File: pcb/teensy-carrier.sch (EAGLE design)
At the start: 13 parts

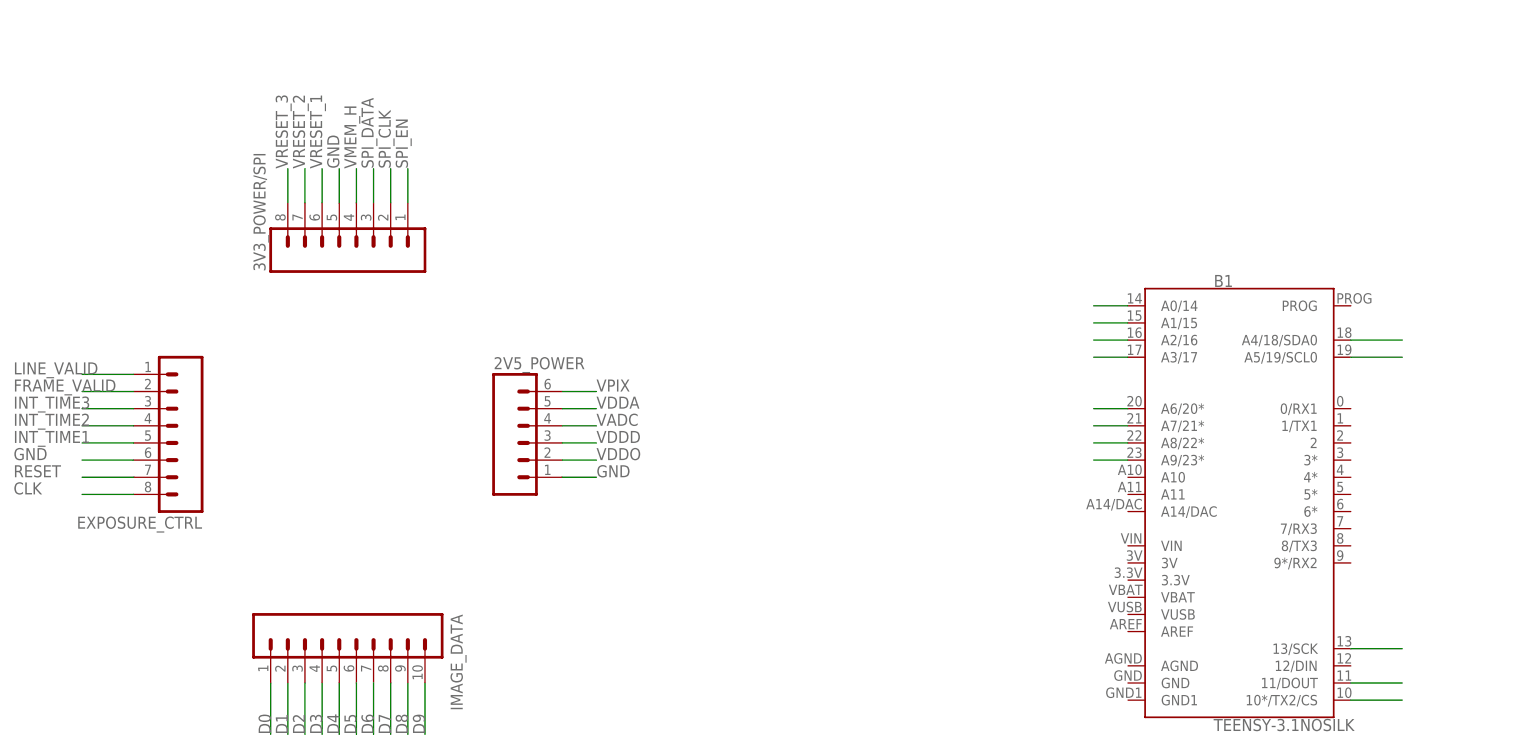
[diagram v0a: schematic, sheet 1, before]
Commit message: finished teensy carrier and added image of dimensions
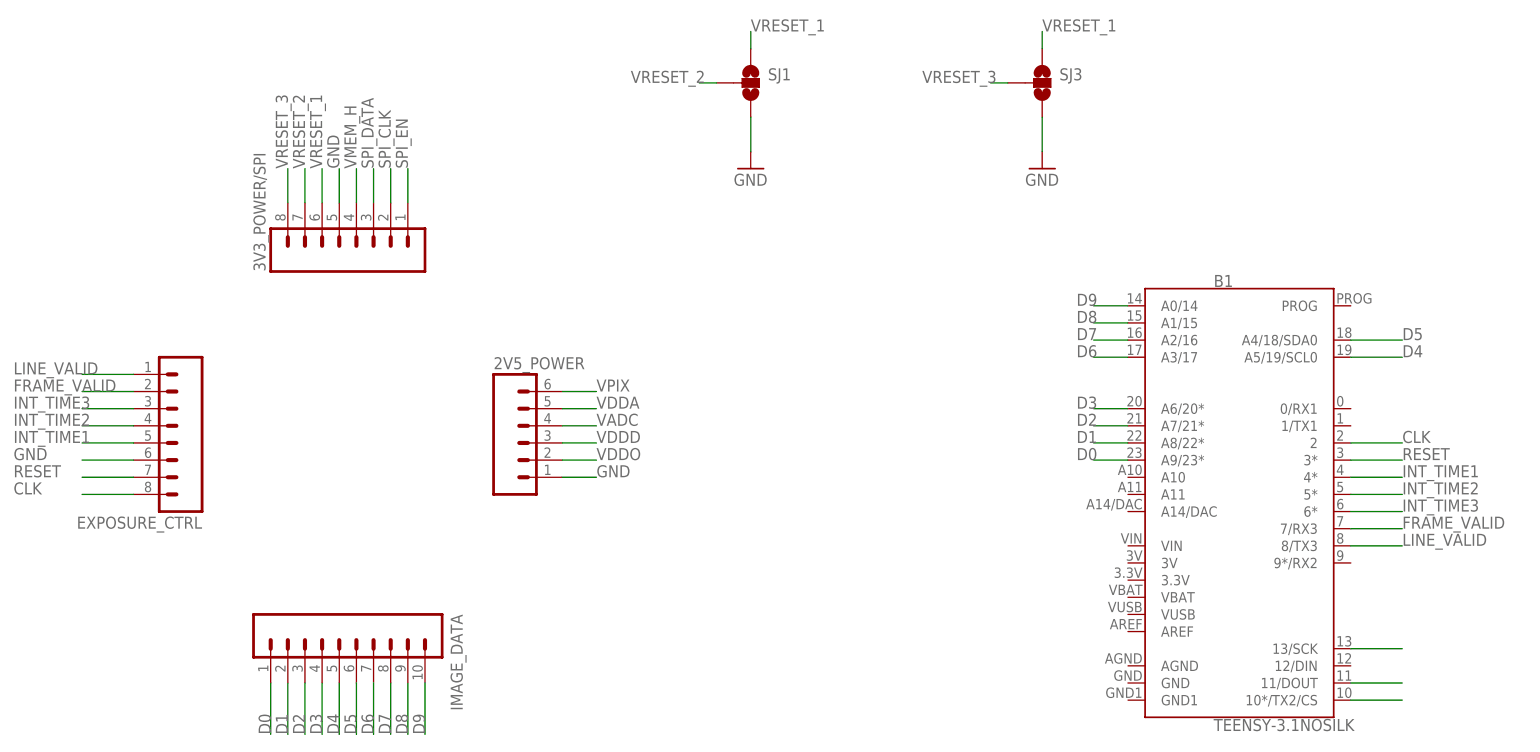
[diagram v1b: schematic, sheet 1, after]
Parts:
- added SJ1, SJ3: (no value), SparkFun-Retired:SOLDERJUMPER_2WAYS
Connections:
- net CLK: now also B1.2
- net FRAME_VALID: now also B1.7/RX3
- net GND: now also SJ1.3, SJ3.3
- net INT_TIME1: now also B1.4*
- net INT_TIME2: now also B1.5*
- net INT_TIME3: now also B1.6*
- net LINE_VALID: now also B1.8/TX3
- net RESET: now also B1.3*
- net VRESET_1: now also SJ1.1, SJ3.1
- net VRESET_2: now also SJ1.2
- net VRESET_3: now also SJ3.2
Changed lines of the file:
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@@
 <?xml version="1.0" encoding="utf-8"?>
 <!DOCTYPE eagle SYSTEM "eagle.dtd">
-<eagle version="8.3.1">
+<eagle version="8.5.0">
 <drawing>
 <settings>
@@
 <part name="GND7" library="SparkFun-Aesthetics" deviceset="GND" device=""/>
 <part name="B1" library="SparkFun-Boards" deviceset="TEENSY-3.1" device="NOSILK"/>
+<part name="SJ1" library="SparkFun-Retired" deviceset="SOLDERJUMPER_2WAY" device="S"/>
+<part name="SJ3" library="SparkFun-Retired" deviceset="SOLDERJUMPER_2WAY" device="S"/>
+<part name="GND3" library="supply1" library_urn="urn:adsk.eagle:library:371" deviceset="GND" device=""/>
+<part name="GND8" library="supply1" library_urn="urn:adsk.eagle:library:371" deviceset="GND" device=""/>
 </parts>
 <sheets>
@@
 <instance part="IMAGE_DATA" gate="G$1" x="58.42" y="22.86" rot="R270"/>
 <instance part="B1" gate="G$1" x="185.42" y="40.64"/>
+<instance part="SJ1" gate="G$1" x="111.76" y="101.6"/>
+<instance part="SJ3" gate="G$1" x="154.94" y="101.6"/>
+<instance part="GND3" gate="1" x="111.76" y="88.9"/>
+<instance part="GND8" gate="1" x="154.94" y="88.9"/>
 </instances>
 <busses>
@@
 <pinref part="B1" gate="G$1" pin="A9/23*"/>
 <wire x1="167.64" y1="45.72" x2="162.56" y2="45.72" width="0.1524" layer="91"/>
+<label x="160.02" y="45.72" size="1.778" layer="95"/>
 </segment>
 </net>
@@
 <pinref part="B1" gate="G$1" pin="A8/22*"/>
 <wire x1="167.64" y1="48.26" x2="162.56" y2="48.26" width="0.1524" layer="91"/>
+<label x="160.02" y="48.26" size="1.778" layer="95"/>
 </segment>
 </net>
@@
 <pinref part="B1" gate="G$1" pin="A7/21*"/>
 <wire x1="167.64" y1="50.8" x2="162.56" y2="50.8" width="0.1524" layer="91"/>
+<label x="160.02" y="50.8" size="1.778" layer="95"/>
 </segment>
 </net>
@@
 <pinref part="B1" gate="G$1" pin="A6/20*"/>
 <wire x1="167.64" y1="53.34" x2="162.56" y2="53.34" width="0.1524" layer="91"/>
+<label x="160.02" y="53.34" size="1.778" layer="95"/>
 </segment>
 </net>
@@
 <pinref part="B1" gate="G$1" pin="A5/19/SCL0"/>
 <wire x1="200.66" y1="60.96" x2="208.28" y2="60.96" width="0.1524" layer="91"/>
+<label x="208.28" y="60.96" size="1.778" layer="95"/>
 </segment>
 </net>
@@
 <pinref part="B1" gate="G$1" pin="A4/18/SDA0"/>
 <wire x1="200.66" y1="63.5" x2="208.28" y2="63.5" width="0.1524" layer="91"/>
+<label x="208.28" y="63.5" size="1.778" layer="95"/>
 </segment>
 </net>
@@
 <pinref part="B1" gate="G$1" pin="A3/17"/>
 <wire x1="167.64" y1="60.96" x2="162.56" y2="60.96" width="0.1524" layer="91"/>
+<label x="160.02" y="60.96" size="1.778" layer="95"/>
 </segment>
 </net>
@@
 <pinref part="B1" gate="G$1" pin="A2/16"/>
 <wire x1="167.64" y1="63.5" x2="162.56" y2="63.5" width="0.1524" layer="91"/>
+<label x="160.02" y="63.5" size="1.778" layer="95"/>
 </segment>
 </net>
@@
 <pinref part="B1" gate="G$1" pin="A1/15"/>
 <wire x1="167.64" y1="66.04" x2="162.56" y2="66.04" width="0.1524" layer="91"/>
+<label x="160.02" y="66.04" size="1.778" layer="95"/>
 </segment>
 </net>
@@
 <pinref part="B1" gate="G$1" pin="A0/14"/>
 <wire x1="167.64" y1="68.58" x2="162.56" y2="68.58" width="0.1524" layer="91"/>
+<label x="160.02" y="68.58" size="1.778" layer="95"/>
 </segment>
 </net>
@@
 <label x="2.54" y="40.64" size="1.778" layer="95"/>
 </segment>
+<segment>
+<pinref part="B1" gate="G$1" pin="2"/>
+<wire x1="200.66" y1="48.26" x2="208.28" y2="48.26" width="0.1524" layer="91"/>
+<label x="208.28" y="48.26" size="1.778" layer="95"/>
+</segment>
 </net>
 <net name="RESET" class="0">
@@
 <label x="2.54" y="43.18" size="1.778" layer="95"/>
 </segment>
+<segment>
+<pinref part="B1" gate="G$1" pin="3*"/>
+<wire x1="200.66" y1="45.72" x2="208.28" y2="45.72" width="0.1524" layer="91"/>
+<label x="208.28" y="45.72" size="1.778" layer="95"/>
+</segment>
 </net>
 <net name="GND" class="0">
@@
 <label x="50.8" y="88.9" size="1.778" layer="95" rot="R90"/>
 </segment>
+<segment>
+<pinref part="SJ1" gate="G$1" pin="3"/>
+<wire x1="111.76" y1="96.52" x2="111.76" y2="91.44" width="0.1524" layer="91"/>
+<pinref part="GND3" gate="1" pin="GND"/>
+</segment>
+<segment>
+<pinref part="SJ3" gate="G$1" pin="3"/>
+<wire x1="154.94" y1="96.52" x2="154.94" y2="91.44" width="0.1524" layer="91"/>
+<pinref part="GND8" gate="1" pin="GND"/>
+</segment>
 </net>
 <net name="INT_TIME1" class="0">
@@
 <label x="2.54" y="48.26" size="1.778" layer="95"/>
 </segment>
+<segment>
+<pinref part="B1" gate="G$1" pin="4*"/>
+<wire x1="200.66" y1="43.18" x2="208.28" y2="43.18" width="0.1524" layer="91"/>
+<label x="208.28" y="43.18" size="1.778" layer="95"/>
+</segment>
 </net>
 <net name="INT_TIME2" class="0">
@@
 <label x="2.54" y="50.8" size="1.778" layer="95"/>
 </segment>
+<segment>
+<pinref part="B1" gate="G$1" pin="5*"/>
+<wire x1="200.66" y1="40.64" x2="208.28" y2="40.64" width="0.1524" layer="91"/>
+<label x="208.28" y="40.64" size="1.778" layer="95"/>
+</segment>
 </net>
 <net name="INT_TIME3" class="0">
@@
 <label x="2.54" y="53.34" size="1.778" layer="95"/>
 </segment>
+<segment>
+<pinref part="B1" gate="G$1" pin="6*"/>
+<wire x1="200.66" y1="38.1" x2="208.28" y2="38.1" width="0.1524" layer="91"/>
+<label x="208.28" y="38.1" size="1.778" layer="95"/>
+</segment>
 </net>
 <net name="FRAME_VALID" class="0">
@@
 <label x="2.54" y="55.88" size="1.778" layer="95"/>
 </segment>
+<segment>
+<pinref part="B1" gate="G$1" pin="7/RX3"/>
+<wire x1="200.66" y1="35.56" x2="208.28" y2="35.56" width="0.1524" layer="91"/>
+<label x="208.28" y="35.56" size="1.778" layer="95"/>
+</segment>
 </net>
 <net name="LINE_VALID" class="0">
@@
 <label x="2.54" y="58.42" size="1.778" layer="95"/>
 </segment>
+<segment>
+<pinref part="B1" gate="G$1" pin="8/TX3"/>
+<wire x1="200.66" y1="33.02" x2="208.28" y2="33.02" width="0.1524" layer="91"/>
+<label x="208.28" y="33.02" size="1.778" layer="95"/>
+</segment>
 </net>
 <net name="VPIX" class="0">
@@
 <label x="43.18" y="88.9" size="1.778" layer="95" rot="R90"/>
 </segment>
+<segment>
+<pinref part="SJ3" gate="G$1" pin="2"/>
+<wire x1="149.86" y1="101.6" x2="147.32" y2="101.6" width="0.1524" layer="91"/>
+<label x="137.16" y="101.6" size="1.778" layer="95"/>
+</segment>
 </net>
 <net name="VRESET_2" class="0">
@@
 <label x="45.72" y="88.9" size="1.778" layer="95" rot="R90"/>
 </segment>
+<segment>
+<pinref part="SJ1" gate="G$1" pin="2"/>
+<wire x1="106.68" y1="101.6" x2="104.14" y2="101.6" width="0.1524" layer="91"/>
+<label x="93.98" y="101.6" size="1.778" layer="95"/>
+</segment>
 </net>
 <net name="VRESET_1" class="0">
@@
 <label x="48.26" y="88.9" size="1.778" layer="95" rot="R90"/>
 </segment>
-</net>
+<segment>
+<pinref part="SJ1" gate="G$1" pin="1"/>
+<wire x1="111.76" y1="106.68" x2="111.76" y2="109.22" width="0.1524" layer="91"/>
+<label x="111.76" y="109.22" size="1.778" layer="95"/>
+</segment>
+<segment>
+<pinref part="SJ3" gate="G$1" pin="1"/>
+<wire x1="154.94" y1="106.68" x2="154.94" y2="109.22" width="0.1524" layer="91"/>
+<label x="154.94" y="109.22" size="1.778" layer="95"/>
+</segment>
+</net>
